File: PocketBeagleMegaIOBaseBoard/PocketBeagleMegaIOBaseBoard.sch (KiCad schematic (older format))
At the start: 22 parts, among them J1 RJ45, J2 RJ45, P1 POCKETBEAGLE-P1, P101 0 1, P2 POCKETBEAGLE-P2, T1 + 15 in -, T2 + 15 out -, U1 TCAN332DR, U2 SN65HVD233-HT

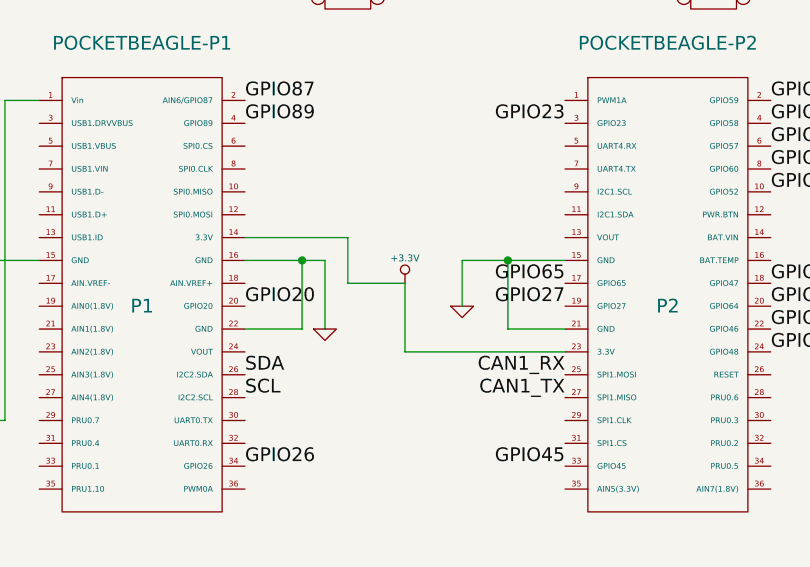
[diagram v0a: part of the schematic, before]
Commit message: Move from I2C2 to I2C1 (reserve I2C2 for eeprom.
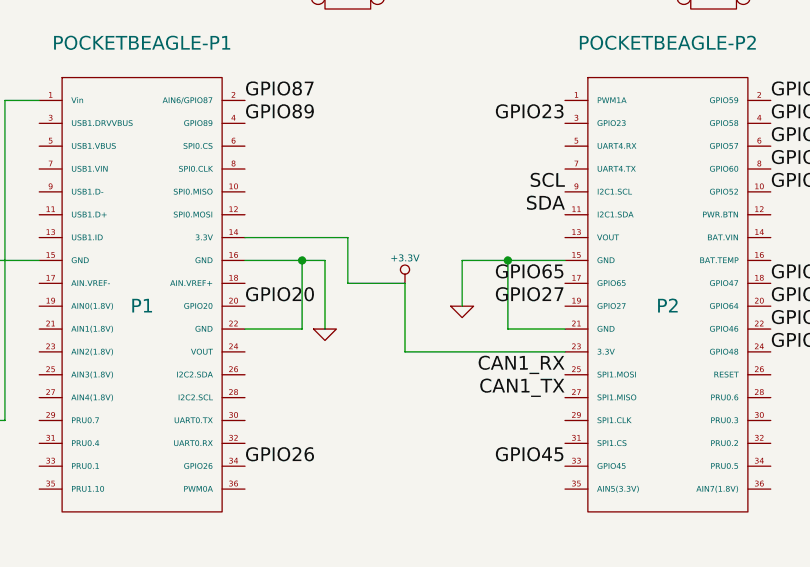
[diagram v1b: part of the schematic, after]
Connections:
- net SCL: now also P2.9 (I2C1.SCL); no longer P1.28 (I2C2.SCL)
- net SDA: now also P2.11 (I2C1.SDA); no longer P1.26 (I2C2.SDA)
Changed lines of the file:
@@
 Sheet 1 4
 Title ""
-Date "7 apr 2019"
+Date "8 jul 2019"
 Rev ""
 Comp ""
@@
 Text Label 8200 950  0    60   ~ 0
 SDA
-Text Label 3300 2850 0    60   ~ 0
+Text Label 4700 2150 2    60   ~ 0
 SDA
-Text Label 3300 2950 0    60   ~ 0
+Text Label 4700 2050 2    60   ~ 0
 SCL
 $Comp

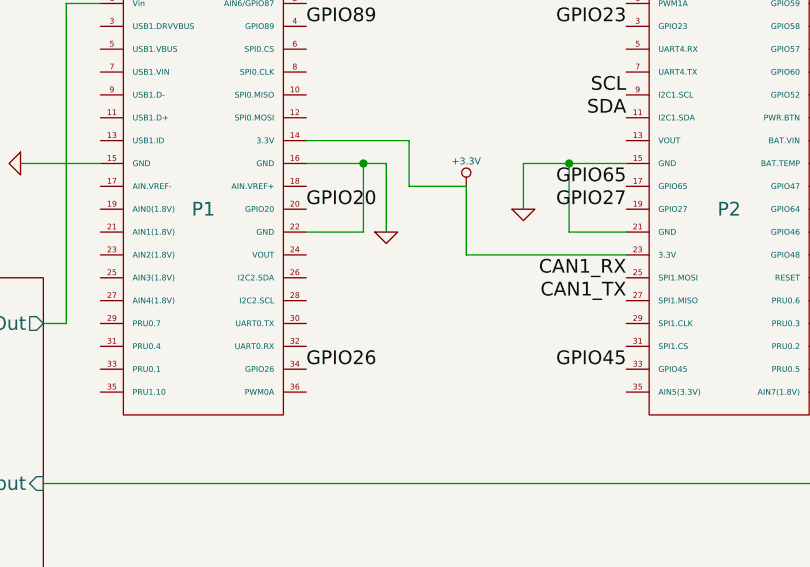
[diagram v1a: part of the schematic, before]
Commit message: Add Console headers to all Pocket Beagle boards.
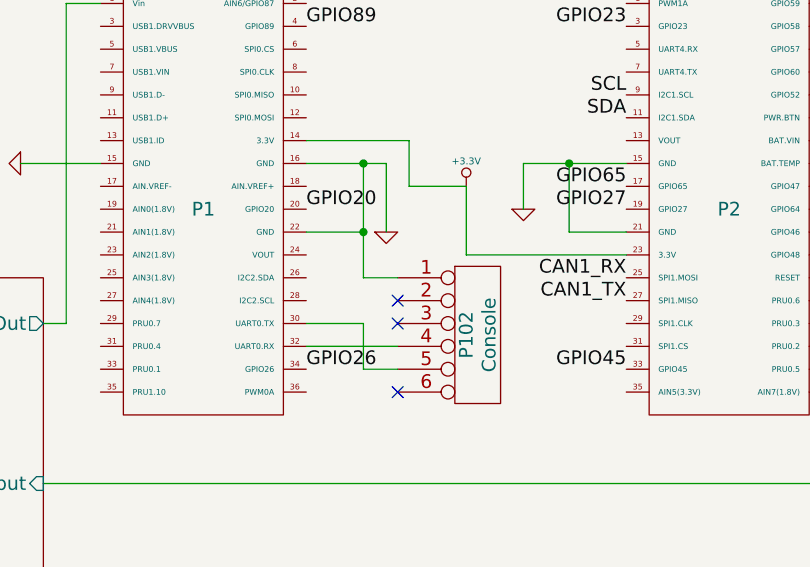
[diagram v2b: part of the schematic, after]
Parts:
- added P102: Console, symbol CONN_6
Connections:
- net GND: now also P102.1
- net at P1.30 (UART0.TX): now also P102.5
- net at P1.32 (UART0.RX): now also P102.4
- no-connect marks 2 -> 5
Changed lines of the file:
@@
 	3300 2650 3550 2650
 Wire Wire Line
-	3550 2650 3550 2350
+	3550 2350 3550 2850
 Connection ~ 3550 2350
 Wire Wire Line
@@
 Connection ~ 9650 1650
 Connection ~ 9650 1800
+$Comp
+L CONN_6 P102
+U 1 1 5D23C4D2
+P 4050 3100
+F 0 "P102" V 4000 3100 60  0000 C CNN
+F 1 "Console" V 4100 3100 60  0000 C CNN
+F 2 "" H 4050 3100 60  0000 C CNN
+F 3 "" H 4050 3100 60  0000 C CNN
+	1    4050 3100
+	1    0    0    -1
+$EndComp
+Wire Wire Line
+	3550 2850 3700 2850
+Connection ~ 3550 2650
+Wire Wire Line
+	3300 3050 3550 3050
+Wire Wire Line
+	3550 3050 3550 3250
+Wire Wire Line
+	3550 3250 3700 3250
+Wire Wire Line
+	3700 3150 3300 3150
+NoConn ~ 3700 2950
+NoConn ~ 3700 3050
+NoConn ~ 3700 3350
 $EndSCHEMATC
